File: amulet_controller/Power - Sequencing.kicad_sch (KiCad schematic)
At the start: 0 parts

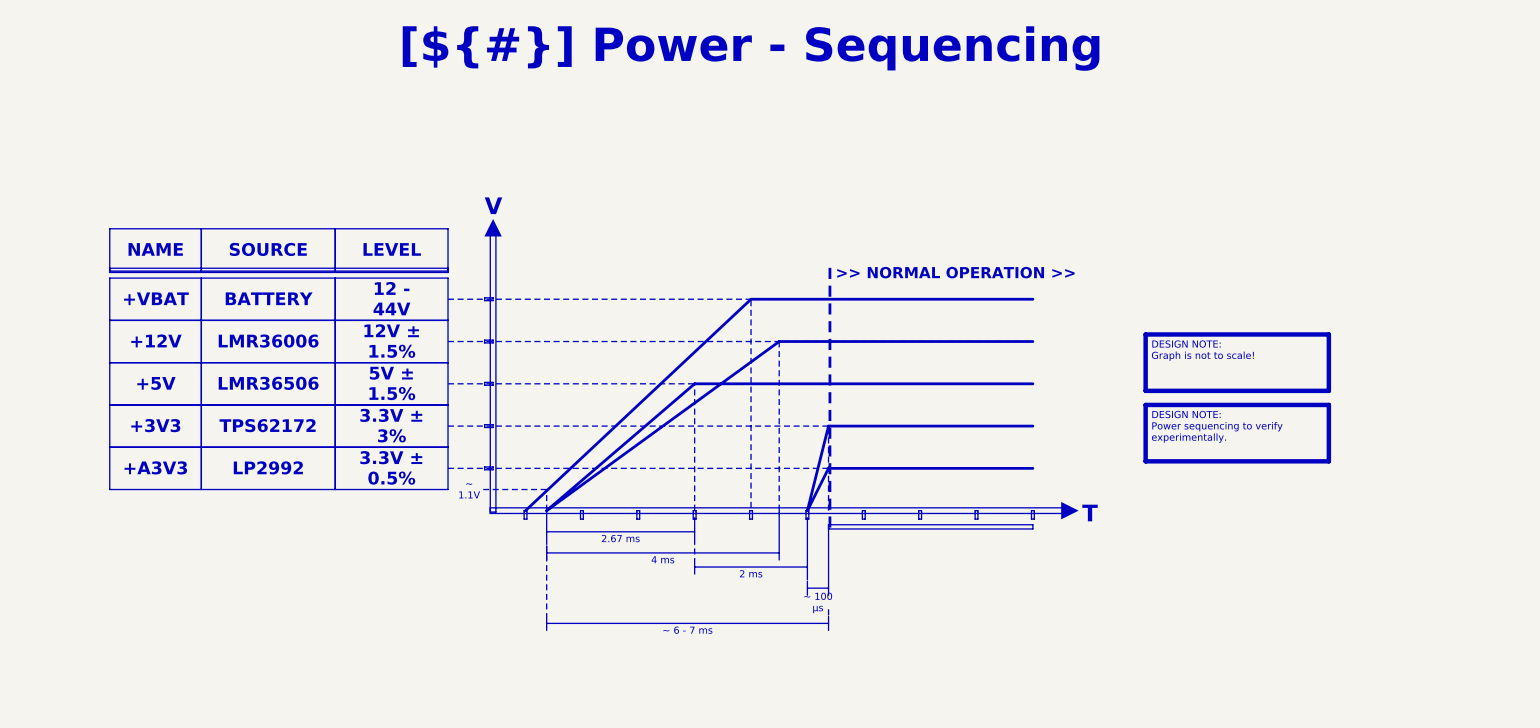
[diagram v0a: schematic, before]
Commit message: modified power sequencing graph and added encoder schematic
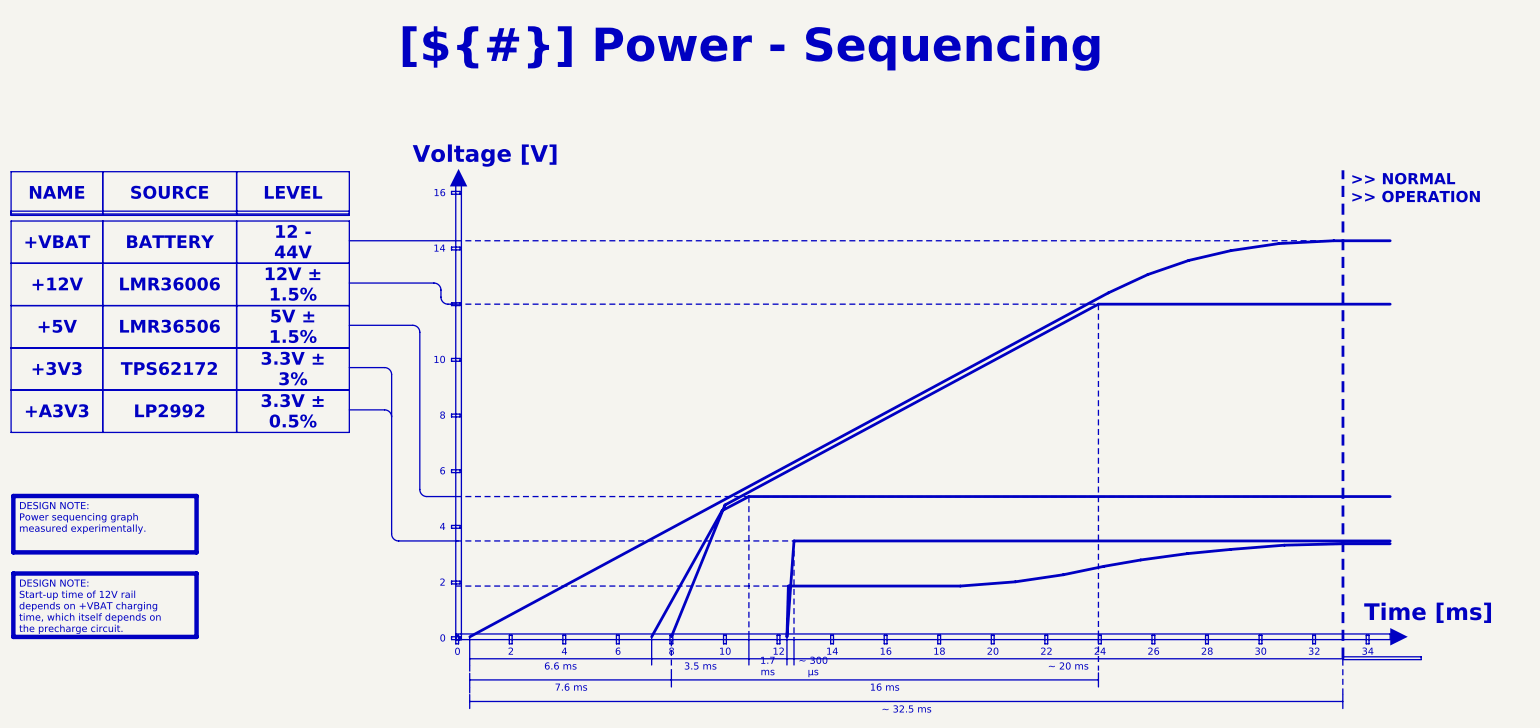
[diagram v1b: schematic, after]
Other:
- note added: ">> NORMAL >> OPERATION"
- note added: "Time [ms]"
- note added: "Voltage [V]"
- note removed: ">> NORMAL OPERATION >>"
- note removed: "T"
- note removed: "V"
